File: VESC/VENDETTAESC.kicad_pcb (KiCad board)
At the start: 6 copper layers, 40.5 x 43 mm, 206 parts, among them J6 SM08B-SRSS-TB, Q1 SP40N03GNJ, Q10 SP40N03GNJ, Q11 SP40N03GNJ, Q12 SP40N03GNJ, Q13 SP40N03GNJ, Q14 SP40N03GNJ, Q15 SP40N03GNJ, Q16 SP40N03GNJ, Q17 SP40N03GNJ, Q18 SP40N03GNJ, Q19 SP40N03GNJ, Q2 SP40N03GNJ, Q20 SP40N03GNJ, Q21 SP40N03GNJ, Q22 SP40N03GNJ, Q23 SP40N03GNJ, Q24 SP40N03GNJ, Q3 SP40N03GNJ, Q4 SP40N03GNJ, Q5 SP40N03GNJ, Q6 SP40N03GNJ, Q7 SP40N03GNJ, Q8 SP40N03GNJ, Q9 SP40N03GNJ, U1 INA185, U10 NSG2065Q, U11 NSG2065Q, U12 VESC, U2 LMR51420YDDCR, U3 TLV76733DRVx, U4 AT32F421G8U7, U5 AT32F421G8U7, U6 AT32F421G8U7, U7 AT32F421G8U7, U8 NSG2065Q, U9 NSG2065Q

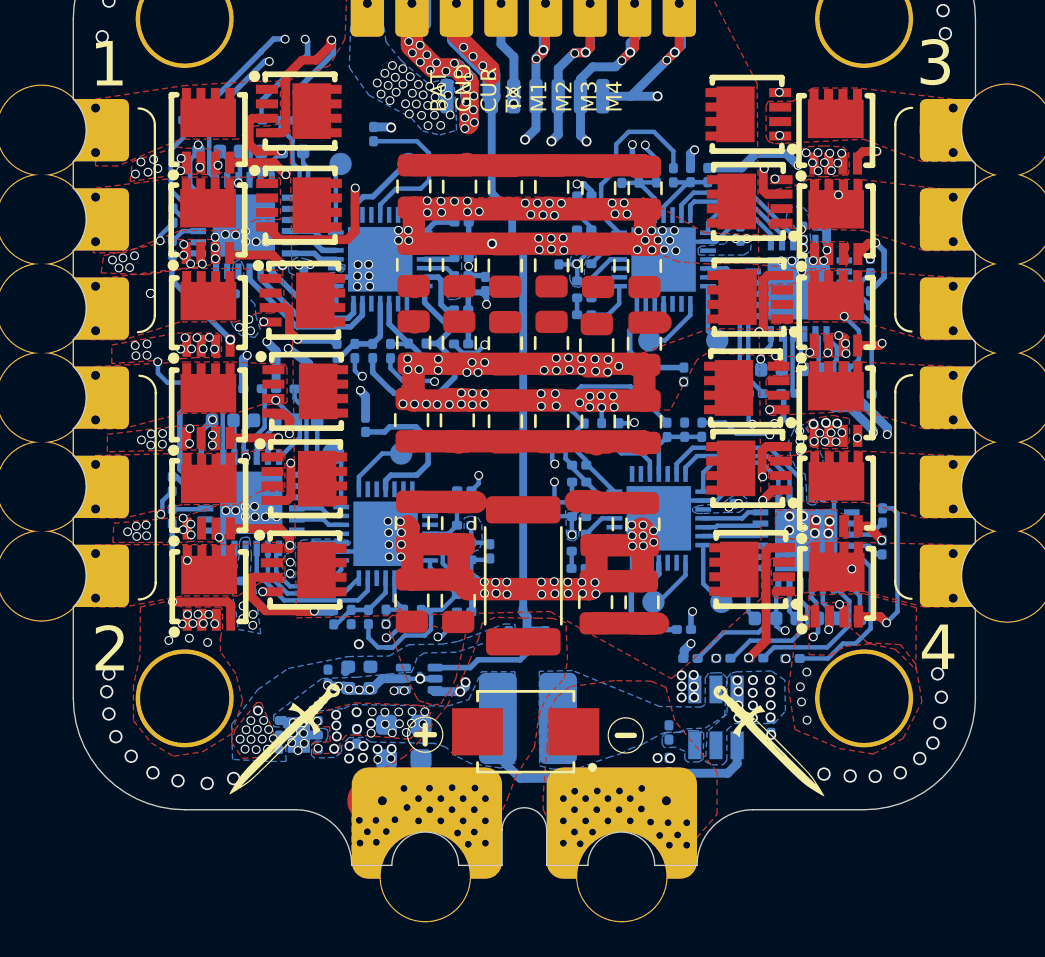
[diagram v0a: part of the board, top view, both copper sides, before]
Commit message: Added telemetery feature for ESC
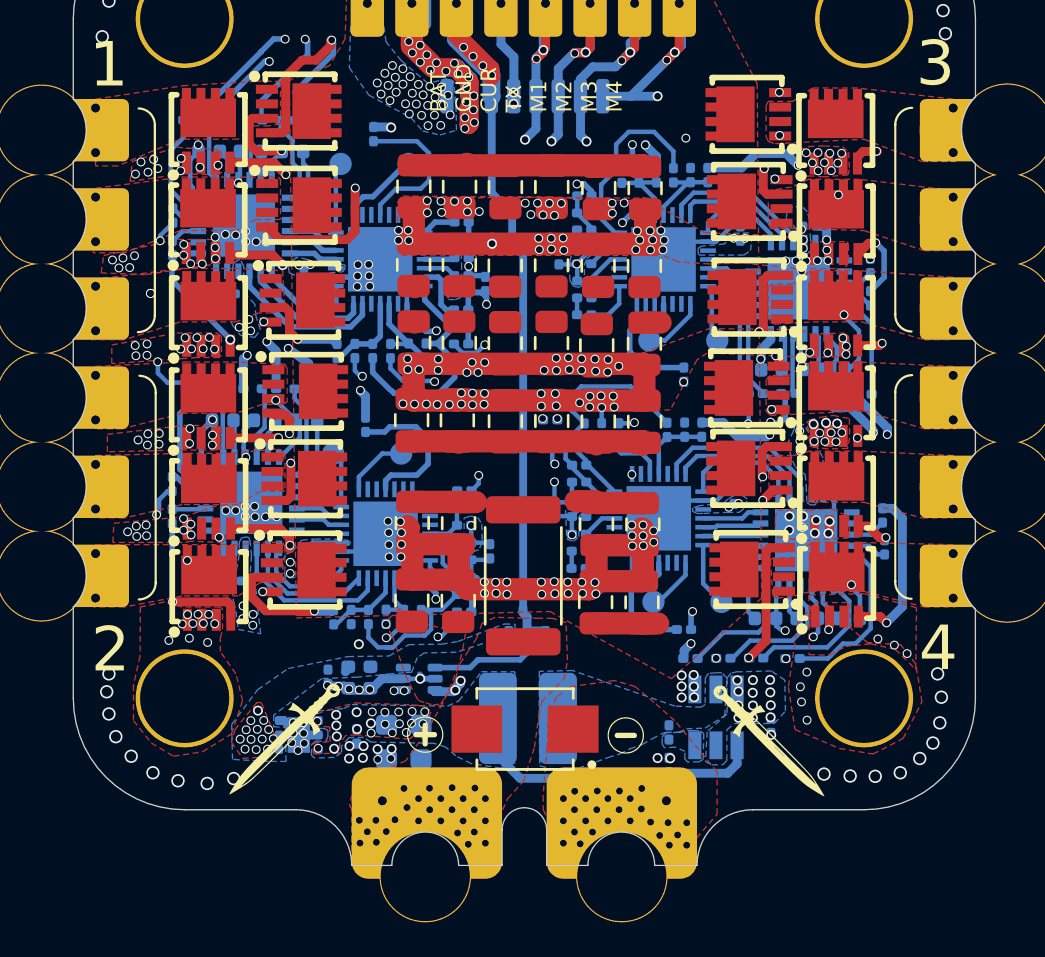
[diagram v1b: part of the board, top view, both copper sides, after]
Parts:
- added R77: 10K, Resistor_SMD:R_0201_0603Metric, B.Cu at (200.9, 103.0)
- L1: value FXL0530-100-M -> 10uH
- moved D1 0.12 mm to (199.8, 116.9)
- moved R68 0.11 mm to (215.9, 108.7)
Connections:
- U4 pad 8: unconnected-(U4-PA2-Pad8) -> TEL
- U5 pad 8: unconnected-(U5-PA2-Pad8) -> TEL
- U6 pad 8: unconnected-(U6-PA2-Pad8) -> TEL
- U7 pad 8: unconnected-(U7-PA2-Pad8) -> TEL
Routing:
- net TEL: track 4.25 -> 54.0 mm, vias 2 -> 7
- net GND: track 141.4 -> 130.2 mm
- net +3.3V: track 105.1 -> 107.0 mm, vias 25 -> 26
- net /CSA+: track 3.45 -> 2.18 mm
- net /ESC3/MOTORB: track 21.4 -> 20.2 mm
- net /ESC4/MOTORC: track 13.2 -> 14.1 mm
- net /ESC4/MOTORA: track 26.6 -> 27.4 mm
